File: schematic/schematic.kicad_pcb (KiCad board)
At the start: 2 copper layers, 71.1 x 55.9 mm, 27 parts, among them J1 BARREL_JACK, J2 CONN_01X17, Q1 BD681, Q10 BD681, Q11 BD681, Q12 BD681, Q13 BD681, Q14 BD681, Q15 BD681, Q16 BD681, Q2 BD681, Q3 BD681, Q4 BD681, Q5 BD681, Q6 BD681, Q7 BD681, Q8 BD681, Q9 BD681, SW1 Optimist, SW2 Pessimist

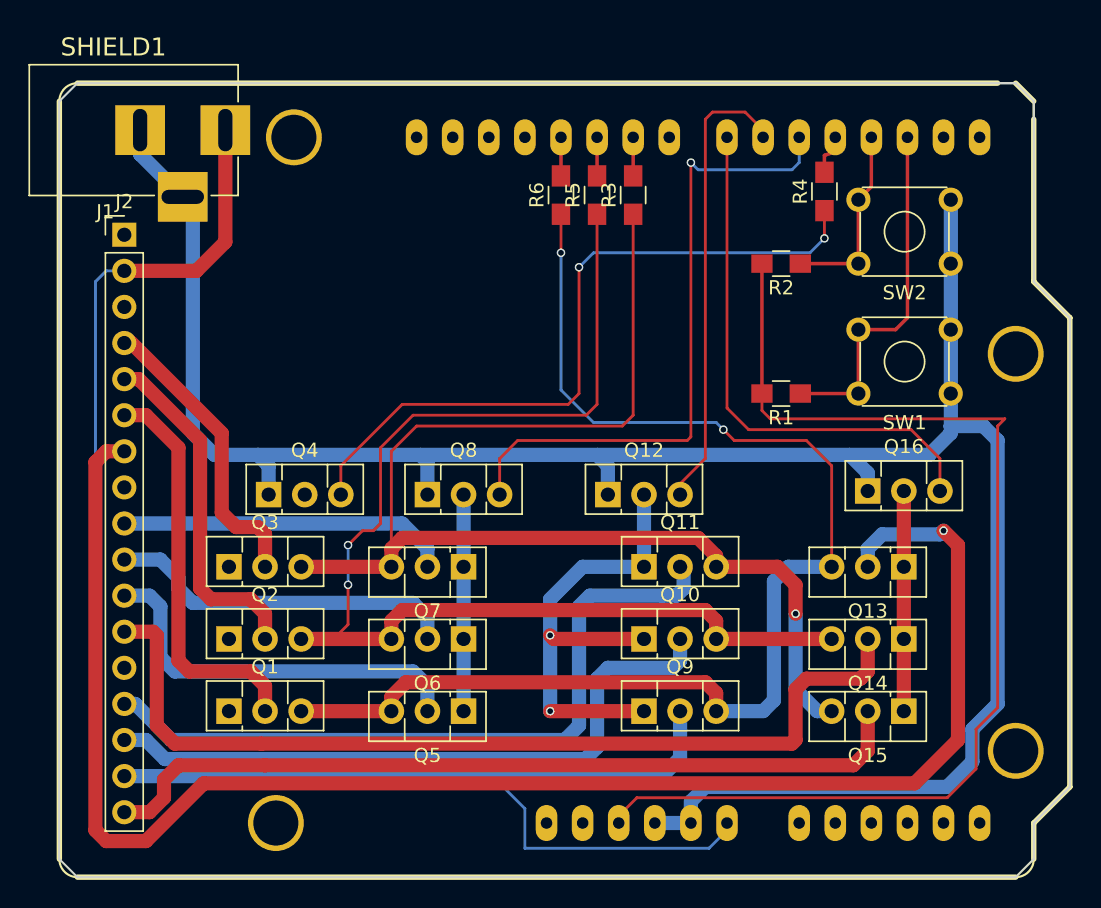
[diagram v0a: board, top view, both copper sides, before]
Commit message: pcb v2 - added resistors, changed connectors, changed tracks
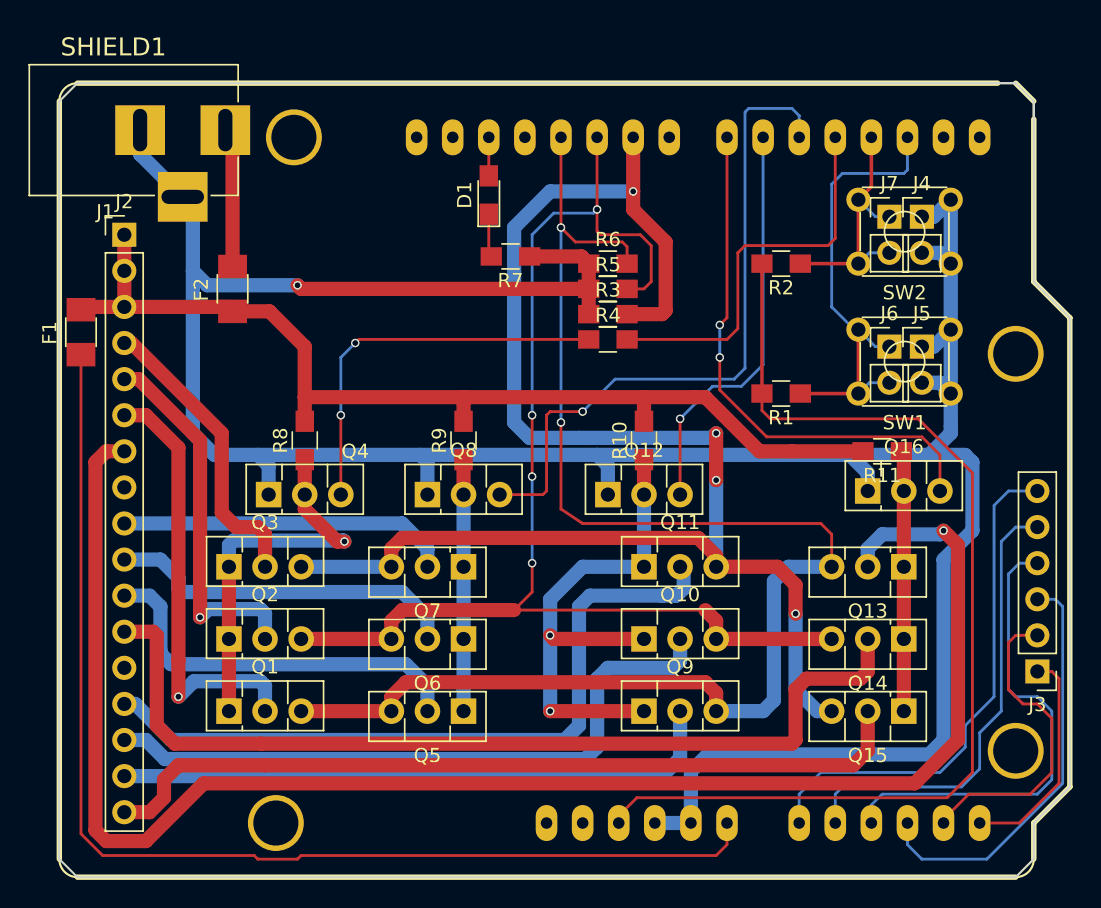
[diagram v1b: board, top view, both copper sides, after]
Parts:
- added D1: LED 13, LEDs:LED_0805_HandSoldering, F.Cu at (114.3, 72.4)
- added F1: 100mAF, Fuse_Holders_and_Fuses:Fuse_SMD1206_Wave, F.Cu at (85.6, 82.0)
- added F2: 1,5AT, Fuse_Holders_and_Fuses:Fuse_SMD1206_Wave, F.Cu at (96.3, 79.0)
- added G***: LOGO, Transfer:minifanti, F.Cu at (106.7, 82.0)
- added J3: CONN_01X06, Pin_Headers:Pin_Header_Straight_1x06_Pitch2.54mm, F.Cu at (152.9, 105.9)
- added J4: CONN_01X02, Pin_Headers:Pin_Header_Straight_1x02_Pitch2.54mm, F.Cu at (144.8, 73.9)
- added J5: CONN_01X02, Pin_Headers:Pin_Header_Straight_1x02_Pitch2.54mm, F.Cu at (144.8, 83.1)
- added J6: CONN_01X02, Pin_Headers:Pin_Header_Straight_1x02_Pitch2.54mm, F.Cu at (142.5, 83.1)
- added J7: , Pin_Headers:Pin_Header_Straight_1x02_Pitch2.54mm, F.Cu at (142.5, 73.9)
- added R10: 10k, Resistors_SMD:R_0805_HandSoldering, F.Cu at (125.2, 89.7)
- added R11: 10k, Resistors_SMD:R_0805_HandSoldering, F.Cu at (142.0, 90.4)
- added R7: 470, Resistors_SMD:R_0805_HandSoldering, F.Cu at (115.8, 76.7)
- added R8: 10k, Resistors_SMD:R_0805_HandSoldering, F.Cu at (101.3, 89.7)
- added R9: 10k, Resistors_SMD:R_0805_HandSoldering, F.Cu at (112.5, 89.7)
- SW1: value Optimist -> D2 Interrupt
- SW2: value Pessimist -> D3 Interrupt
- moved R4 18.5 mm to (122.7, 82.5), turned to 0 degrees
- moved R3 8.57 mm to (122.7, 80.8), turned to 0 degrees
- moved R5 6.65 mm to (122.7, 79.0), turned to 0 degrees
- moved R6 5.85 mm to (122.7, 77.2), turned to 0 degrees
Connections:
- J1 pad 1: +12V -> Net-(F2-Pad2)
- J2 pad 1: Net-(J2-Pad1) -> +12V
- J2 pad 3: Net-(J2-Pad3) -> +12V
- R3 pad 1: Net-(Q11-Pad3) -> GND
- R3 pad 2: Net-(R3-Pad2) -> Net-(Q11-Pad3)
- R5 pad 1: Net-(Q10-Pad3) -> GND
- R5 pad 2: Net-(R5-Pad2) -> Net-(Q10-Pad3)
- R6 pad 1: Net-(Q1-Pad3) -> GND
- R6 pad 2: Net-(R6-Pad2) -> Net-(Q1-Pad3)
- SHIELD1 pad 10: Net-(R5-Pad2) -> Net-(Q10-Pad3)
- SHIELD1 pad 11: Net-(R6-Pad2) -> Net-(Q1-Pad3)
- SHIELD1 pad 9: Net-(R3-Pad2) -> Net-(Q11-Pad3)
- SHIELD1 pad V_IN: +12V -> Net-(F1-Pad1)
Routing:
- net Net-(F1-Pad1): track 0.00 -> 82.4 mm
- net GND: track 158.3 -> 200.8 mm, vias 0 -> 1
- net Net-(J3-Pad6): track 0.00 -> 36.4 mm
- net +12V: track 107.7 -> 72.6 mm
- net Net-(J3-Pad4): track 0.00 -> 33.7 mm
- net Net-(J3-Pad5): track 0.00 -> 32.5 mm
- net Net-(J3-Pad3): track 0.00 -> 29.5 mm
- net Net-(Q1-Pad1): track 0.00 -> 27.2 mm, vias 0 -> 1
- net Net-(R4-Pad2): track 3.01 -> 28.9 mm
- net Net-(Q11-Pad3): track 89.1 -> 112.0 mm, vias 1 -> 4
- net Net-(J3-Pad2): track 0.00 -> 22.5 mm
- net Net-(Q4-Pad3): track 49.9 -> 27.6 mm
- net Net-(J3-Pad1): track 0.00 -> 15.8 mm
- net Net-(Q1-Pad3): track 90.2 -> 104.0 mm
- net Net-(F2-Pad2): track 0.00 -> 10.5 mm
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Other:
- board text added: "+12V"
- board text added: "5V GND"
- board text added: "A0 A1 A2 A3 A4 A5"
- board text added: "MUX1"
- board text added: "MUX2"
- board text added: "MUX3"
- board text added: "MUX4"
- board text added: "fanti"
- board text added: "optipessi shield v2 Marc Fischer"
- board text removed: "optipessi shield v1 Marc Fischer"
